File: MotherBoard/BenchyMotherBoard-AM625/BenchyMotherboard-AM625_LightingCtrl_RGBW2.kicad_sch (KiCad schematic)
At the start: 13 parts, among them J21 B5B-XH-A, Q10 PMXB43UNEZ, Q11 PMXB43UNEZ, Q12 PMXB43UNEZ, Q9 PMXB43UNEZ

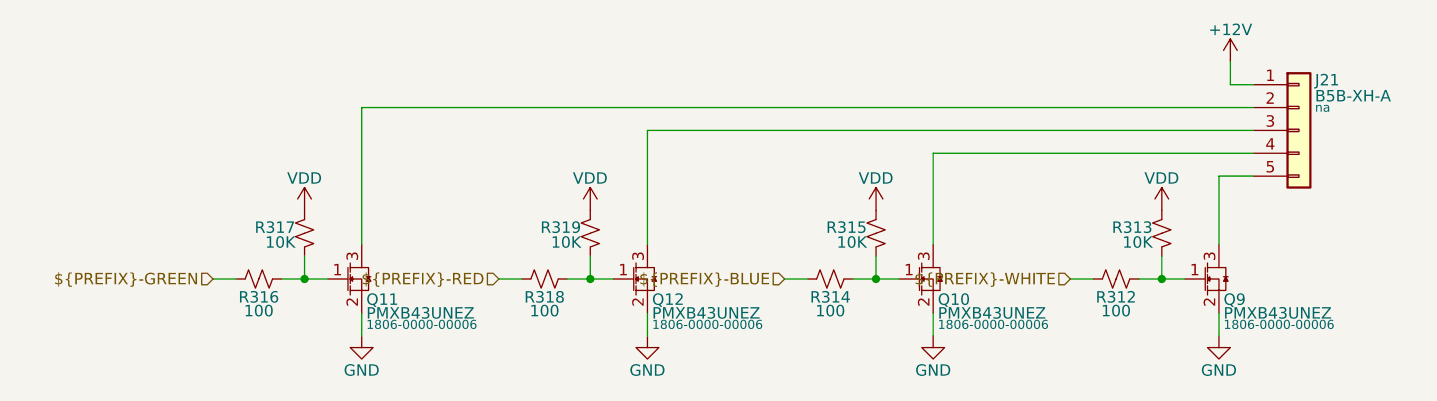
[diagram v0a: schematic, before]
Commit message: Schematic capture mostly complete. Starting PCB layout
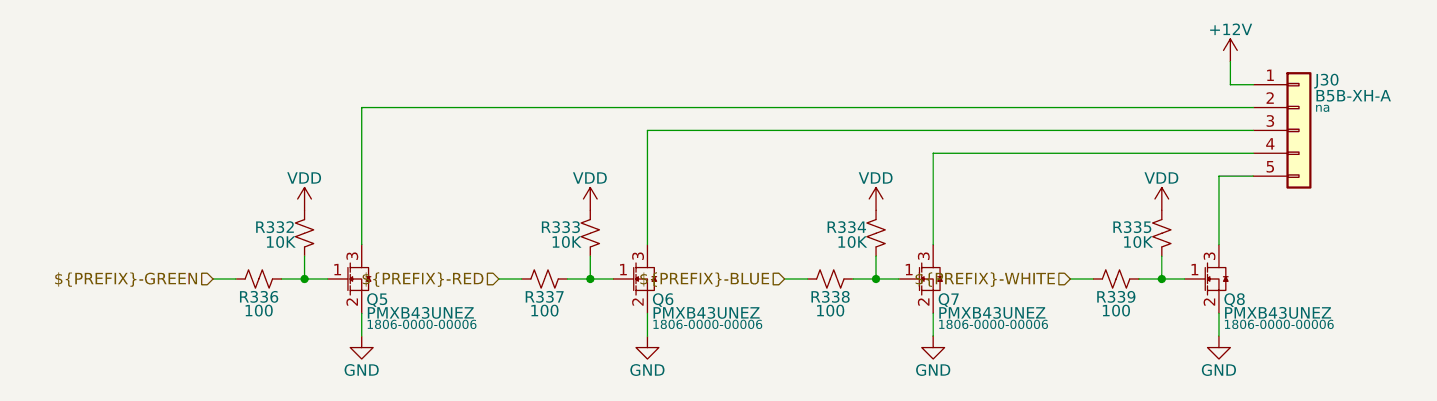
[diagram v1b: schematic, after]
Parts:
- removed J21: B5B-XH-A, Daxxn_Connectors_JST:B5B-XH-A, symbol DX_Connector_JST:B5B-XH-A
- removed Q10, Q11, Q12, Q9: PMXB43UNEZ, Daxxn_Packages:DFN1010D-3, symbol DX_Transistor_MOSFET:PMXB43UNEZ
- removed R312, R314, R316, R318: 100, Daxxn_Standard_Resistors:RES_0402, symbol DX_Resistor:RC0402JR-07100RL
- removed R313, R315, R317, R319: 10K, Daxxn_Standard_Resistors:RES_0402, symbol DX_Resistor:RC0402JR-0710KL
- added J30: B5B-XH-A, Daxxn_Connectors_JST:B5B-XH-A, symbol DX_Connector_JST:B5B-XH-A
- added Q5, Q6, Q7, Q8: PMXB43UNEZ, Daxxn_Packages:DFN1010D-3, symbol DX_Transistor_MOSFET:PMXB43UNEZ
- added R332, R333, R334, R335: 10K, Daxxn_Standard_Resistors:RES_0402, symbol DX_Resistor:RC0402JR-0710KL
- added R336, R337, R338, R339: 100, Daxxn_Standard_Resistors:RES_0402, symbol DX_Resistor:RC0402JR-07100RL
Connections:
- net ${PREFIX}-BLUE: now also R338.1
- net ${PREFIX}-GREEN: now also R336.1
- net ${PREFIX}-RED: now also R337.1
- net ${PREFIX}-WHITE: now also R339.1
- net +12V: now also J30.1 (Pin_1)
- net GND: now also Q5.2 (S), Q6.2 (S), Q7.2 (S), Q8.2 (S)
- net VDD: now also R332.1, R333.1, R334.1, R335.1
- new net: Q5.1 (G), R332.2, R336.2
- new net: Q6.1 (G), R333.2, R337.2
- new net: Q7.1 (G), R334.2, R338.2
- new net: J30.2 (Pin_2), Q5.3 (D)
- new net: Q8.1 (G), R335.2, R339.2
- new net: J30.5 (Pin_5), Q8.3 (D)
- new net: J30.4 (Pin_4), Q7.3 (D)
- new net: J30.3 (Pin_3), Q6.3 (D)
